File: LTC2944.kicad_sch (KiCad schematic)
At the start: 1 part, among them U1 LTC2944IDD#PBF

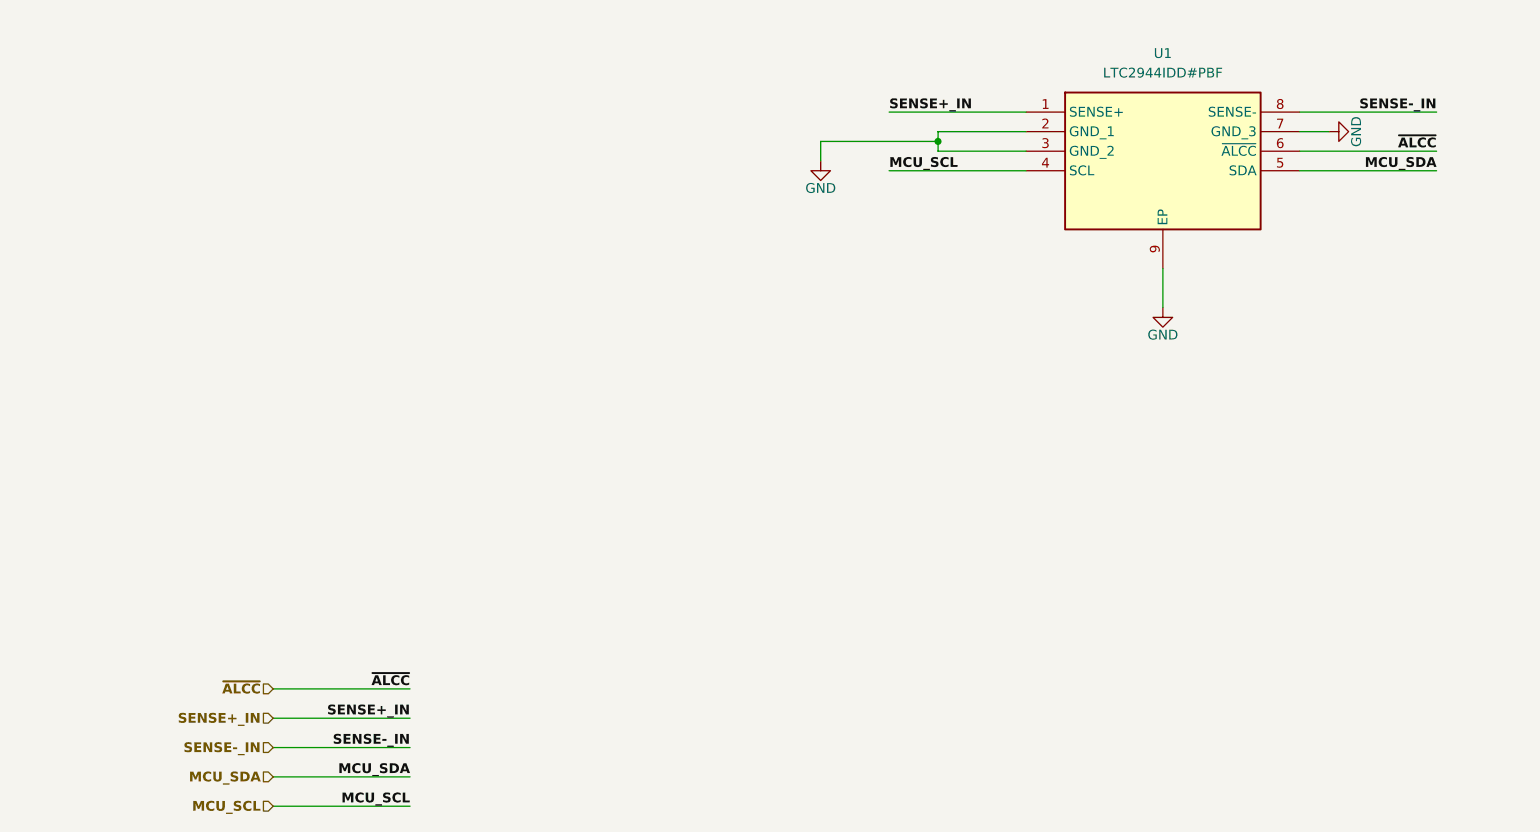
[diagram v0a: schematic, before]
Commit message: Assigned footprints
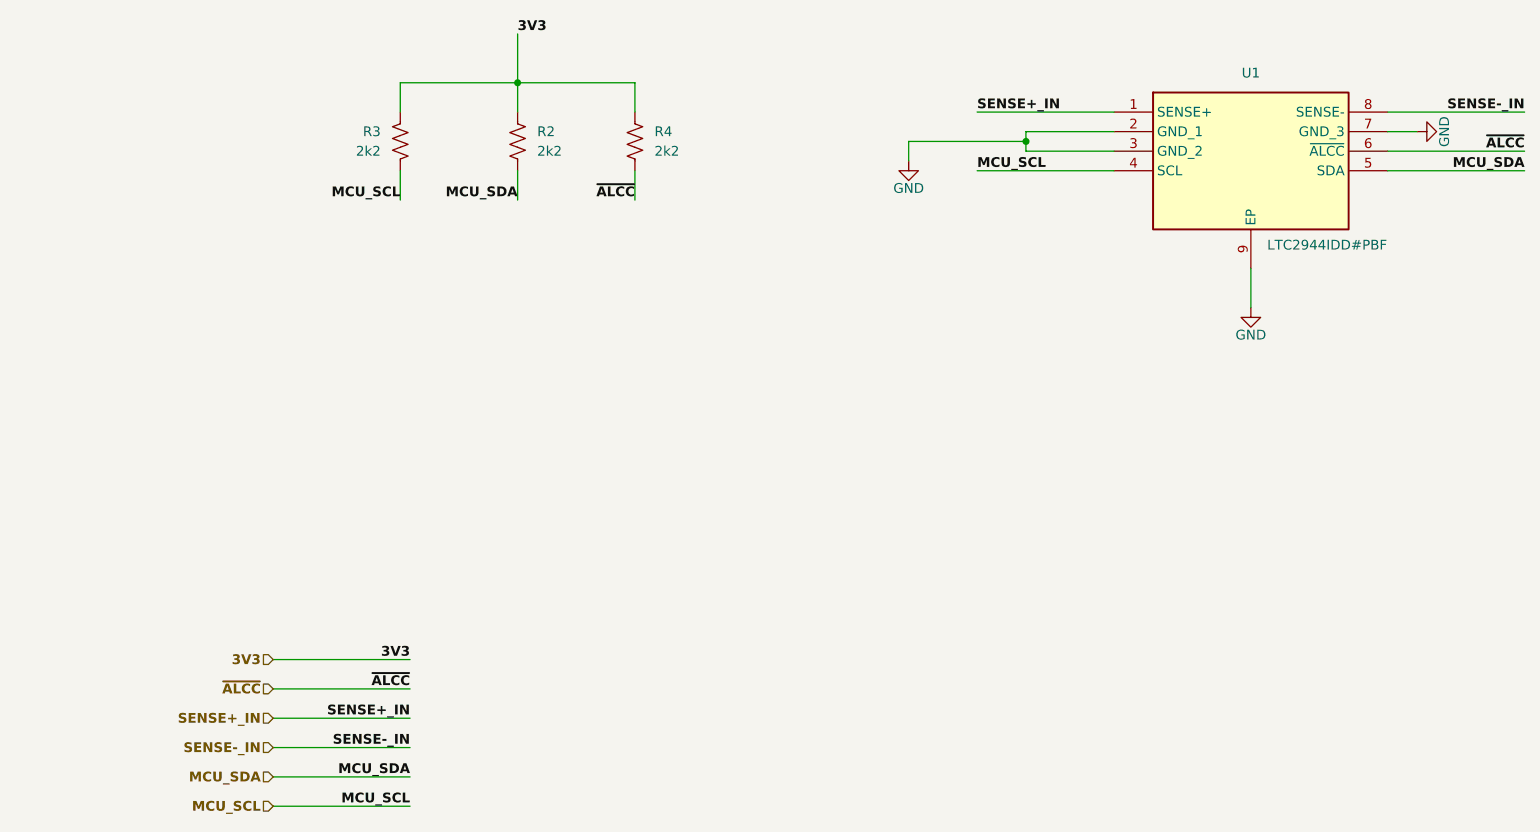
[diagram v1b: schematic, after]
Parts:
- added R2, R3, R4: 2k2, PP_PoC:R_0402_1005Metric_Pad0.72x0.64mm_HandSolder, symbol PP_PoC:R_US
- U1: footprint SON50P300X300X80-9N-D -> PP_PoC:LTC2944_DFN; Arrow Part Number LTC2944IDD#PBF -> (none); Arrow Price/Stock https://www.arrow.com/en/products/ltc2944iddpbf/analog-devi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 -> (none); Height 0.8 -> (none); Manufacturer_Name Analog Devices -> (none); Manufacturer_Part_Number LTC2944IDD#PBF -> (none); Mouser Part Number 584-LTC2944IDDPBF -> (none); Mouser Price/Stock https://www.mouser.co.uk/ProductDetail/Analog-Devices/LTC29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 -> (none); PN (none) -> LTC2944IDD#PBF
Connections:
- net MCU_SCL: now also R3.2
- net MCU_SDA: now also R2.2
- net ~{ALCC}: now also R4.2
- new net 3V3: R2.1, R3.1, R4.1
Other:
- moved on the sheet: U1

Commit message: Started routing
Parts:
- added C1: 1uF, PP_PoC:C_0603_1608Metric_Pad1.08x0.95mm_HandSolder, symbol PP_PoC:C
- R2, R3, R4: value 2k2 -> 2k; PN RC0402FR-072K2L -> WR04X2001FTL
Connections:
- net GND: now also C1.1
- net SENSE+_IN: now also C1.2
- net 3V3 renamed 3V3/5V
- net MCU_SCL renamed SCL
- net SCL: now also R2.2; no longer R3.2
- net MCU_SDA renamed SDA
- net SDA: now also R3.2; no longer R2.2
